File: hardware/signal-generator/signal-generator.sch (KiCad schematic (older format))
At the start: 39 parts, among them J1 AVR-ISP-6, J10 Output_Conn, J2 AVR_SPI, J3 AREF, J4 PORT_G, J5 PORT_F, J6 PORT_E, J7 PORT_A, J8 PORT_C, J9 Power_Supply_Rails, SW1 RESET_BUTTON, U1 74HC04, U2 74HC08, U3 74HC08, U4 74HC30, U5 ATmega2561-16AU, U6 ADP7142AUJZ-5.0, U7 TC1017-3.3VCTTR, Y1 16MHz

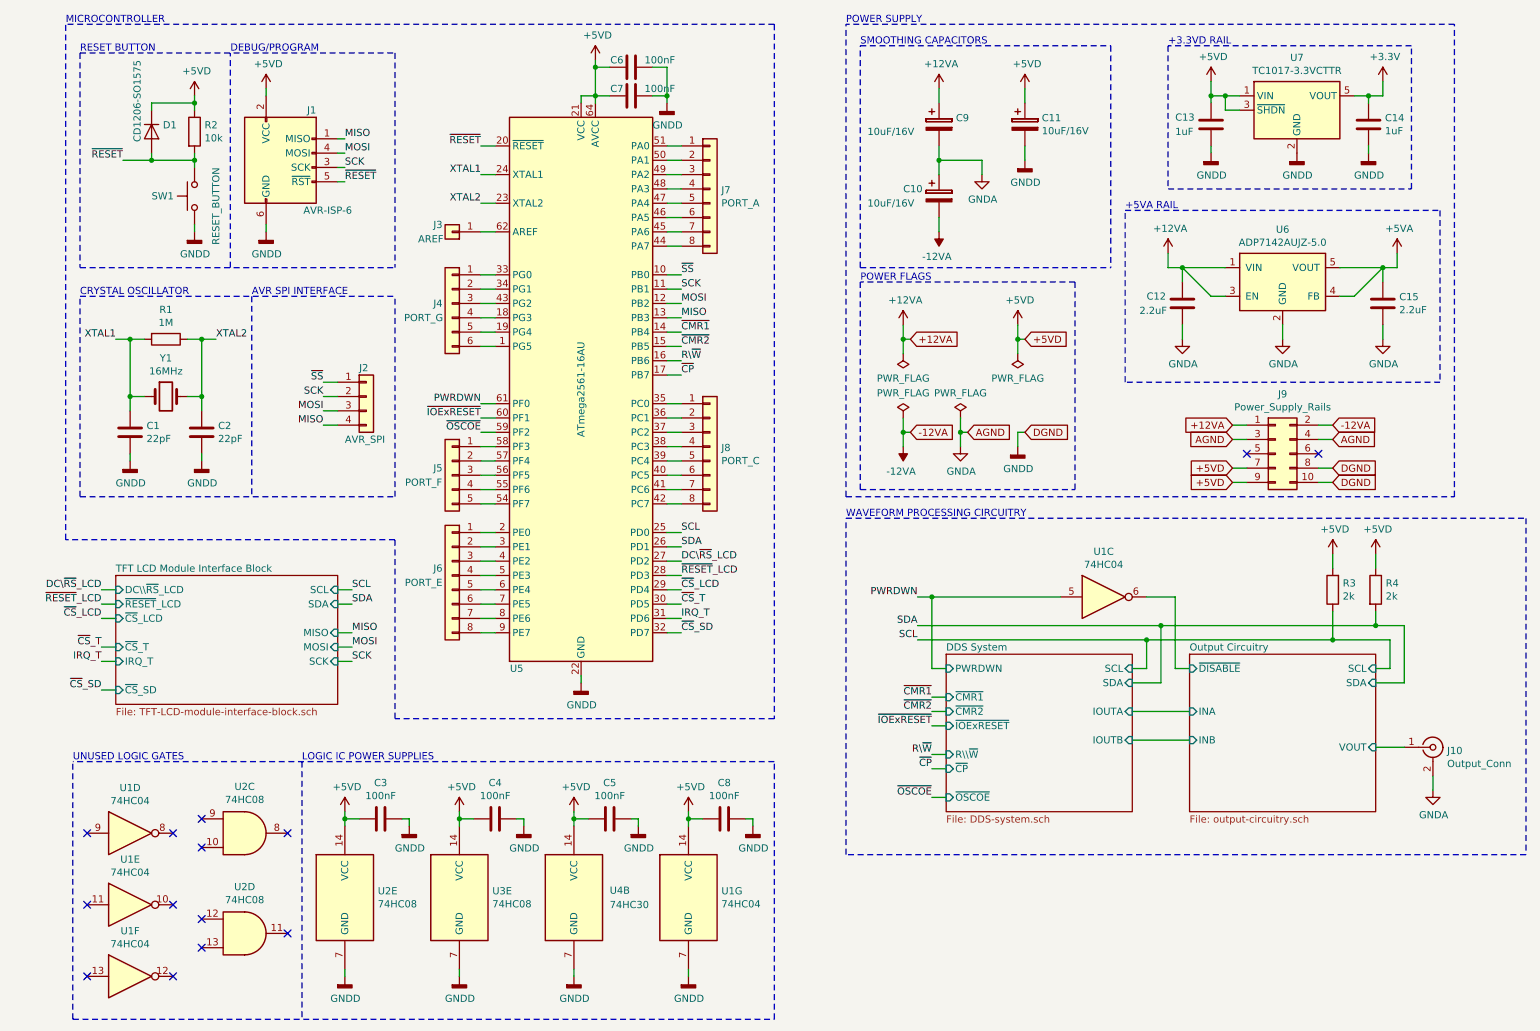
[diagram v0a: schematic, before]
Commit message: [Signal Generator] Change LCD backlight control method
The LCD's backlight was previously intended to be controlled via a
digital potentiometer. However, a much more elegant solution is to
control said backlight via PWM.

Also, removed the level shifter schematic sheet. The level shifters have been
moved to the TFT module's schematic sheet.
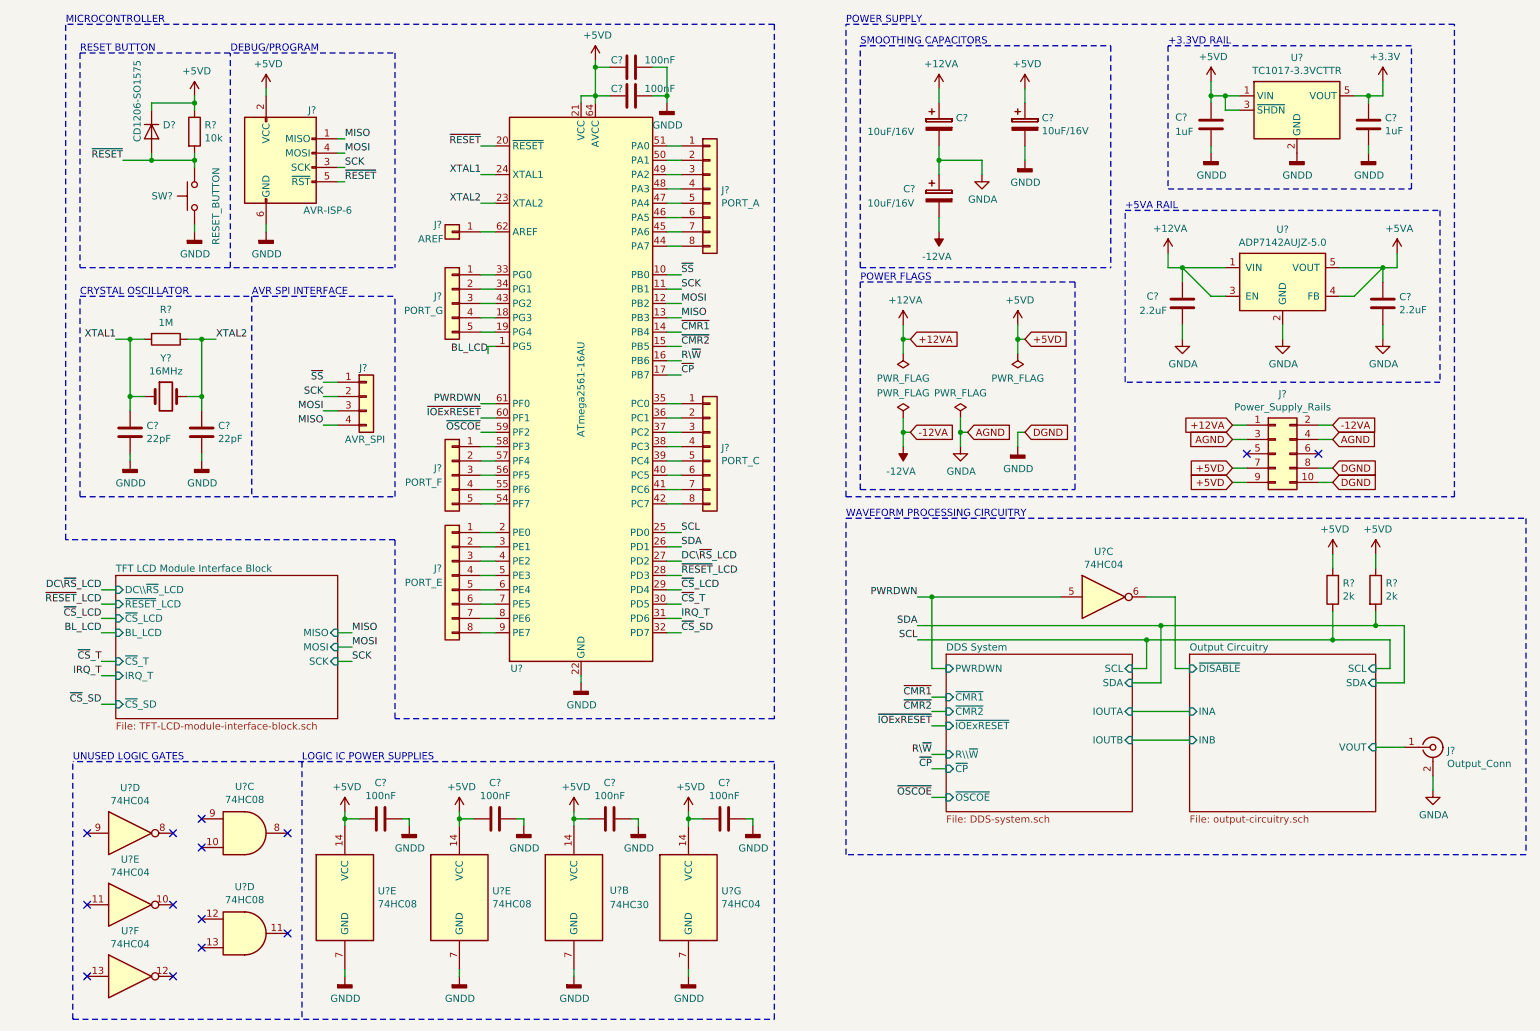
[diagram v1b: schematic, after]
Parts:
- removed J4: PORT_G, Pin_Headers:Pin_Header_Straight_1x06_Pitch2.54mm, symbol Connector_Generic:Conn_01x06
- added J?: PORT_G, symbol Connector_Generic:Conn_01x05
- renumbered C11 to C?, C9 to C?, C10 to C?, C15 to C?, C12 to C?, C7 to C?, C6 to C?, C1 to C?, C2 to C?, C13 to C?, C14 to C?, C3 to C?, C4 to C?, C5 to C?, C8 to C?, D1 to D?, J9 to J?, J1 to J?, J10 to J?, J5 to J?, J7 to J?, J8 to J?, J2 to J?, J6 to J?, J3 to J?, R2 to R?, R1 to R?, R4 to R?, R3 to R?, SW1 to SW?, U6 to U?, U5 to U?, U4 to U?, U3 to U?, U2 to U?, U1 to U?, U7 to U?, Y1 to Y?
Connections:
- net BL_LCD: now reaches U?.1 (PG5)
- net at U?.18 (PG3): now also J?.4 (Pin_4)
- net at U?.19 (PG4): now also J?.5 (Pin_5)
- net at U?.33 (PG0): now also J?.1 (Pin_1)
- net at U?.34 (PG1): now also J?.2 (Pin_2)
- net at U?.43 (PG2): now also J?.3 (Pin_3)

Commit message: [Signal Generator] Minor changes
1) Decouple AREF to GNDD with 100nF capacitor. The ATmega's internal ADC
will be used to calibrate the output circuitry's digital potentiometers.

2) Change I2C address of output DC offset digital potentiometer
(MCP4551) from '0101 111' to '0101 110'.
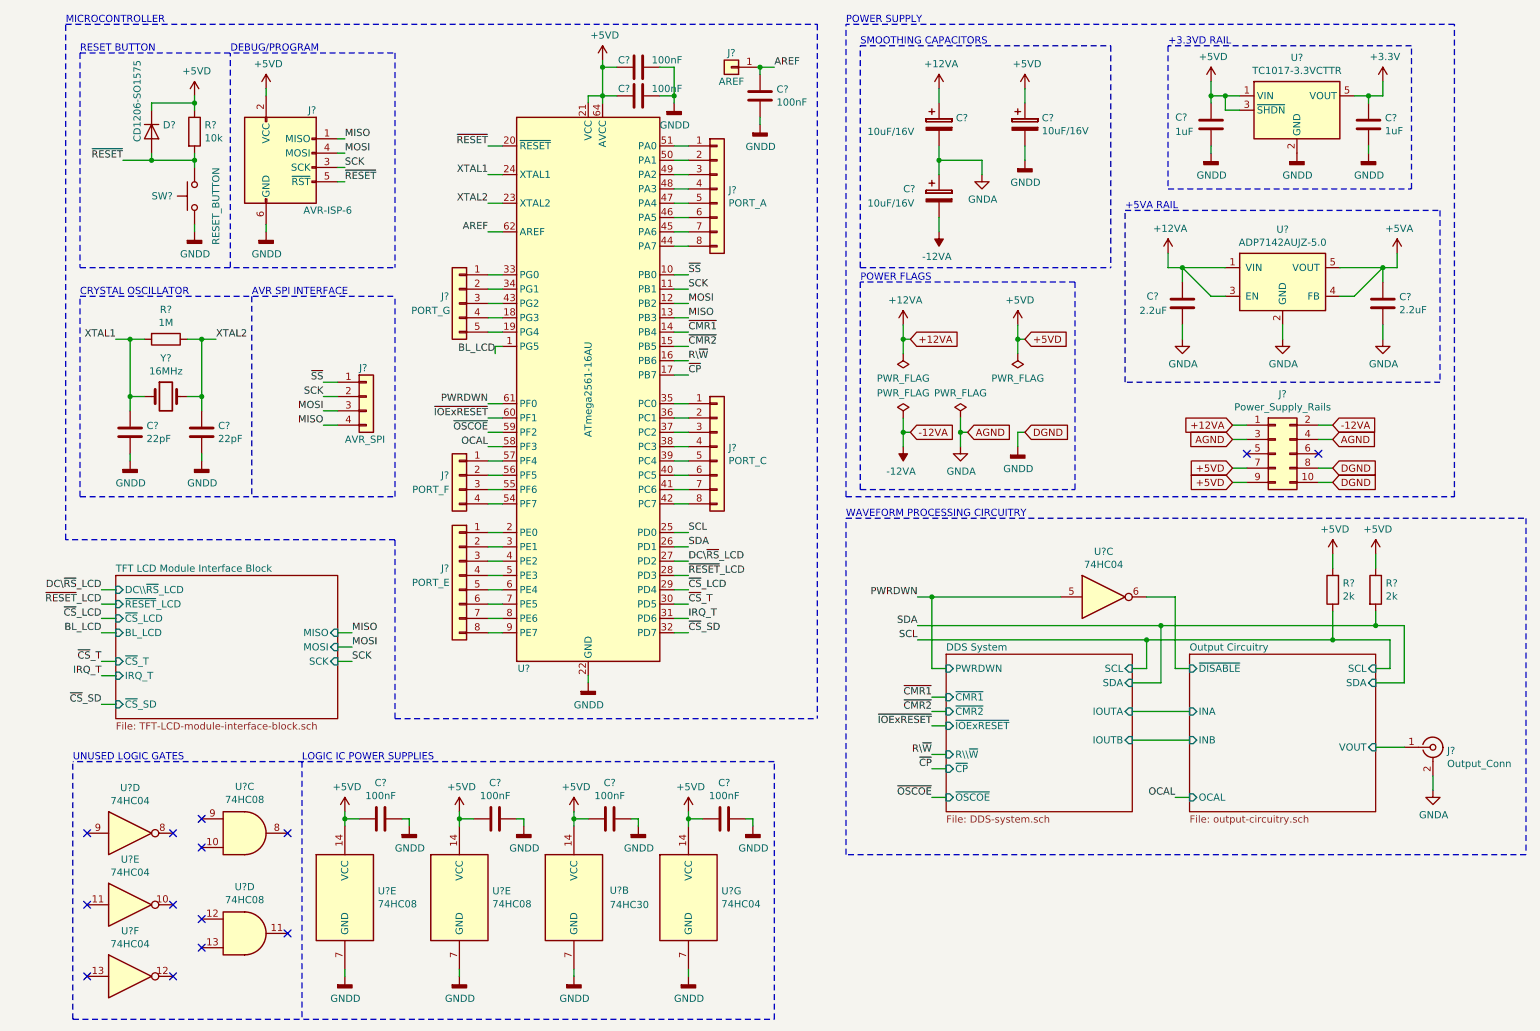
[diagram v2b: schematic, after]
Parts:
- removed J?: PORT_F, Pin_Headers:Pin_Header_Straight_1x05_Pitch2.54mm, symbol Connector_Generic:Conn_01x05
- added C?: 100nF, symbol Device:C
- added J?: PORT_F, symbol Connector_Generic:Conn_01x04
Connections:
- net GNDD: now also C?.2
- net at U?.54 (PF7): now also J?.4 (Pin_4)
- net at U?.55 (PF6): now also J?.3 (Pin_3)
- net at U?.56 (PF5): now also J?.2 (Pin_2)
- net at U?.57 (PF4): now also J?.1 (Pin_1)
- net OCAL: now reaches U?.58 (PF3)
- net AREF: now reaches J?.1 (Pin_1), U?.62 (AREF)
- net AREF: now also C?.1
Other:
- moved on the sheet: C?, J?, U?

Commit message: [Signal Generator] Finalize schematic
The electronic schematic is now finalized. All components have been
annotated. Furthermore, all components have an appropriate footprint
associated to them.
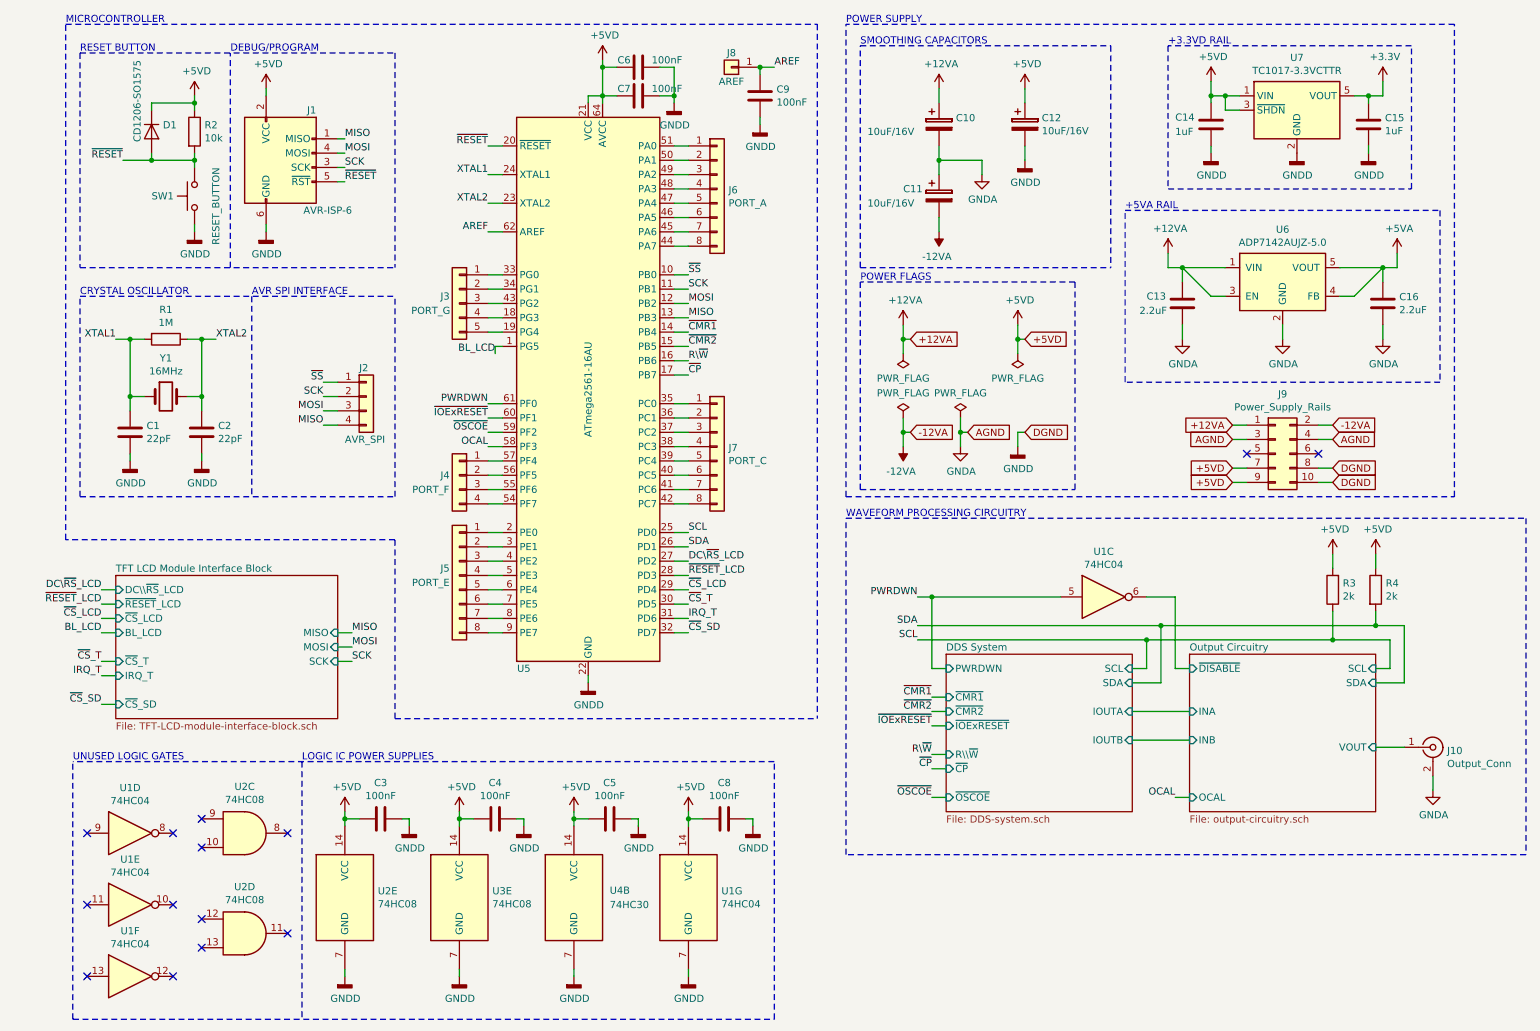
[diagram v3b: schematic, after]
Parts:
- C9: renamed from C?; footprint (none) -> Capacitors_SMD:C_0805_HandSoldering
- J3: renamed from J?; footprint (none) -> Pin_Headers:Pin_Header_Straight_1x05_Pitch2.54mm
- J4: renamed from J?; footprint (none) -> Pin_Headers:Pin_Header_Straight_1x04_Pitch2.54mm
- gave numbers to parts that had none: 37
